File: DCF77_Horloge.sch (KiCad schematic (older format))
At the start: 22 parts, among them J1 USB_B_Micro, J2 Conn_SWD, J3 Conn_Display, J4 Conn_DCF, Q1 AO3401A, U1 MCP73831-2-OT, U2 NCP1117-3.3_SOT223

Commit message: Add pull up for i2c and change layout
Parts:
- added R8, R9: 2K, Resistor_SMD:R_0603_1608Metric_Pad1.05x0.95mm_HandSolder, symbol Device:R
- J1: symbol Connector:USB_B_Micro -> DCF77_Horloge-rescue:USB_B_Micro-Connector
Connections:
- wire segments 54 -> 60
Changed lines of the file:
@@
 	3350 2350 3700 2350
 $Comp
-L Connector:USB_B_Micro J1
+L DCF77_Horloge-rescue:USB_B_Micro-Connector J1
 U 1 1 6115A94F
 P 1050 1900
@@
 	0    1    1    0
 $EndComp
+Text GLabel 8950 1450 2    50   Input ~ 0
+SCL
+Text GLabel 8950 1350 2    50   Input ~ 0
+SDA
+$Comp
+L Device:R R9
+U 1 1 611EA76E
+P 8850 1150
+F 0 "R9" H 8800 1100 50  0000 R CNN
+F 1 "2K" H 8780 1195 50  0000 R CNN
+F 2 "Resistor_SMD:R_0603_1608Metric_Pad1.05x0.95mm_HandSolder" V 8780 1150 50  0001 C CNN
+F 3 "~" H 8850 1150 50  0001 C CNN
+	1    8850 1150
+	-1   0    0    1
+$EndComp
+$Comp
+L Device:R R8
+U 1 1 611EB153
+P 8600 1150
+F 0 "R8" H 8750 1150 50  0000 R CNN
+F 1 "2K" H 8750 1250 50  0000 R CNN
+F 2 "Resistor_SMD:R_0603_1608Metric_Pad1.05x0.95mm_HandSolder" V 8530 1150 50  0001 C CNN
+F 3 "~" H 8600 1150 50  0001 C CNN
+	1    8600 1150
+	-1   0    0    1
+$EndComp
+Wire Wire Line
+	8850 1300 8850 1350
+Wire Wire Line
+	8850 1350 8950 1350
+Wire Wire Line
+	8950 1450 8600 1450
+Wire Wire Line
+	8600 1450 8600 1300
+Wire Wire Line
+	8600 1000 8750 1000
+$Comp
+L power:+3.3V #PWR011
+U 1 1 611EE2A2
+P 8750 1000
+F 0 "#PWR011" H 8750 850 50  0001 C CNN
+F 1 "+3.3V" H 8750 1100 50  0000 L CNN
+F 2 "" H 8750 1000 50  0001 C CNN
+F 3 "" H 8750 1000 50  0001 C CNN
+	1    8750 1000
+	1    0    0    -1
+$EndComp
+Connection ~ 8750 1000
+Wire Wire Line
+	8750 1000 8850 1000
 $EndSCHEMATC

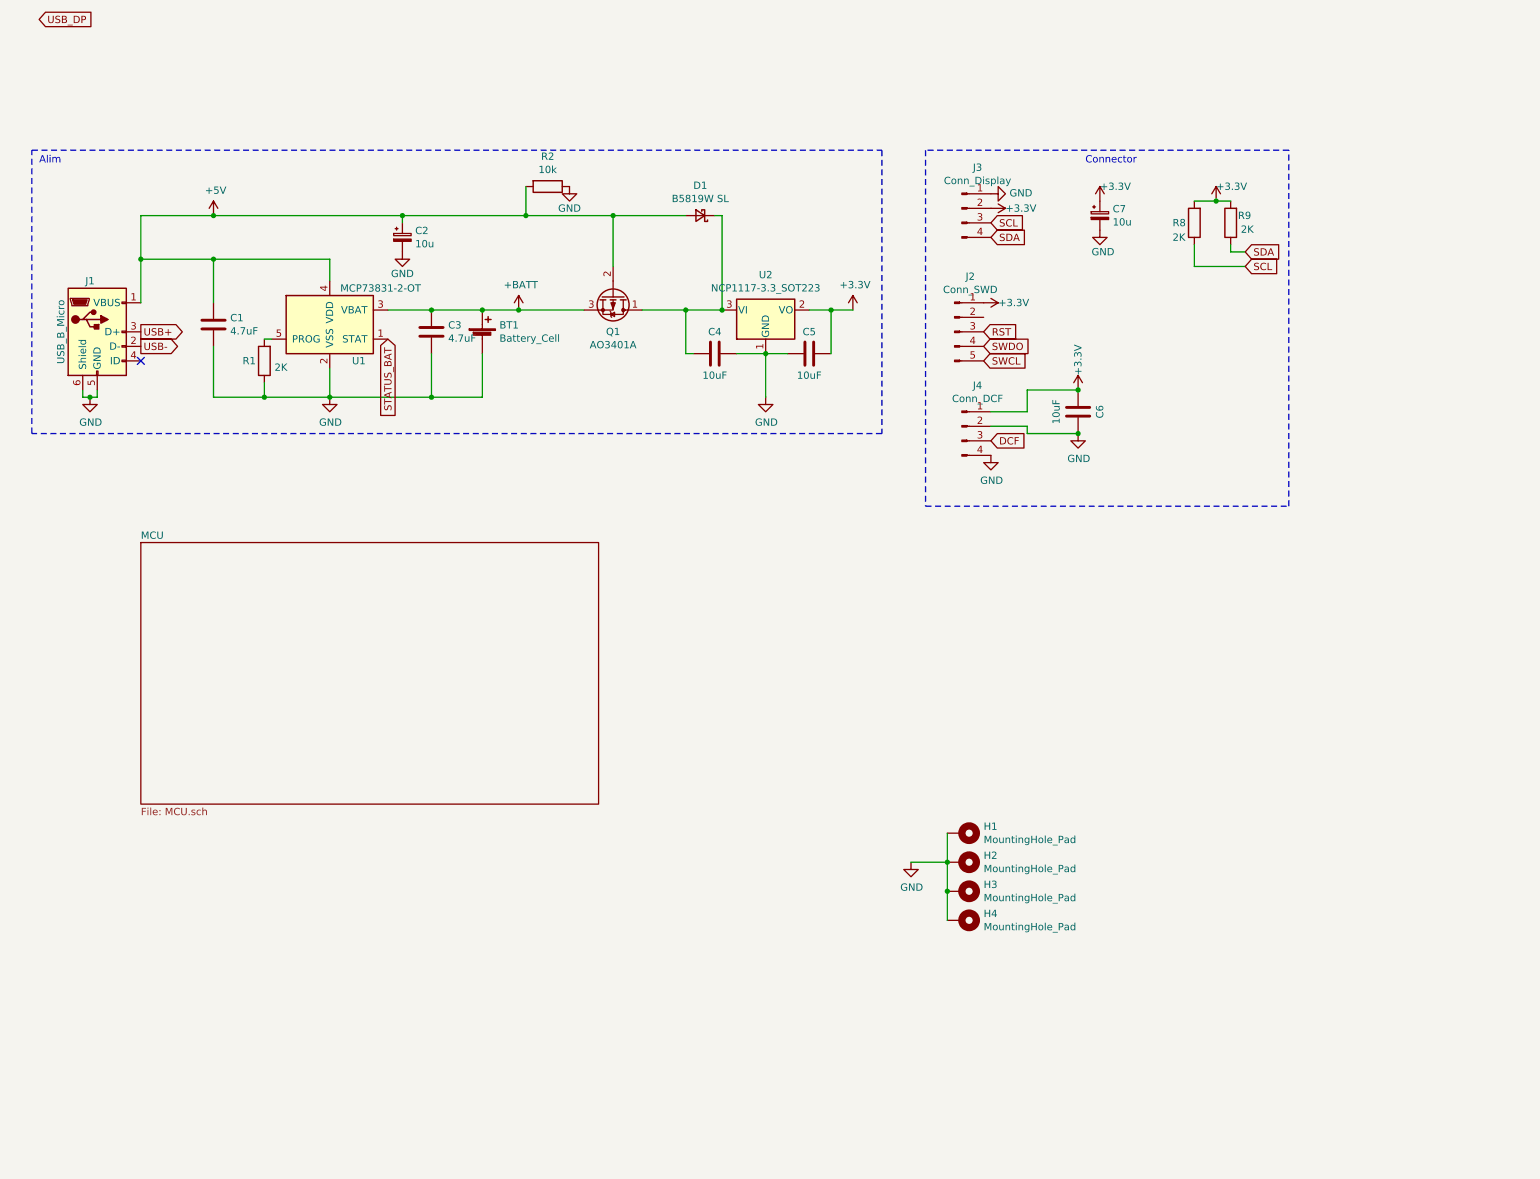
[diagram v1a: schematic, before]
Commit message: change MCU from RP2040 to ESP32-WROOM-32
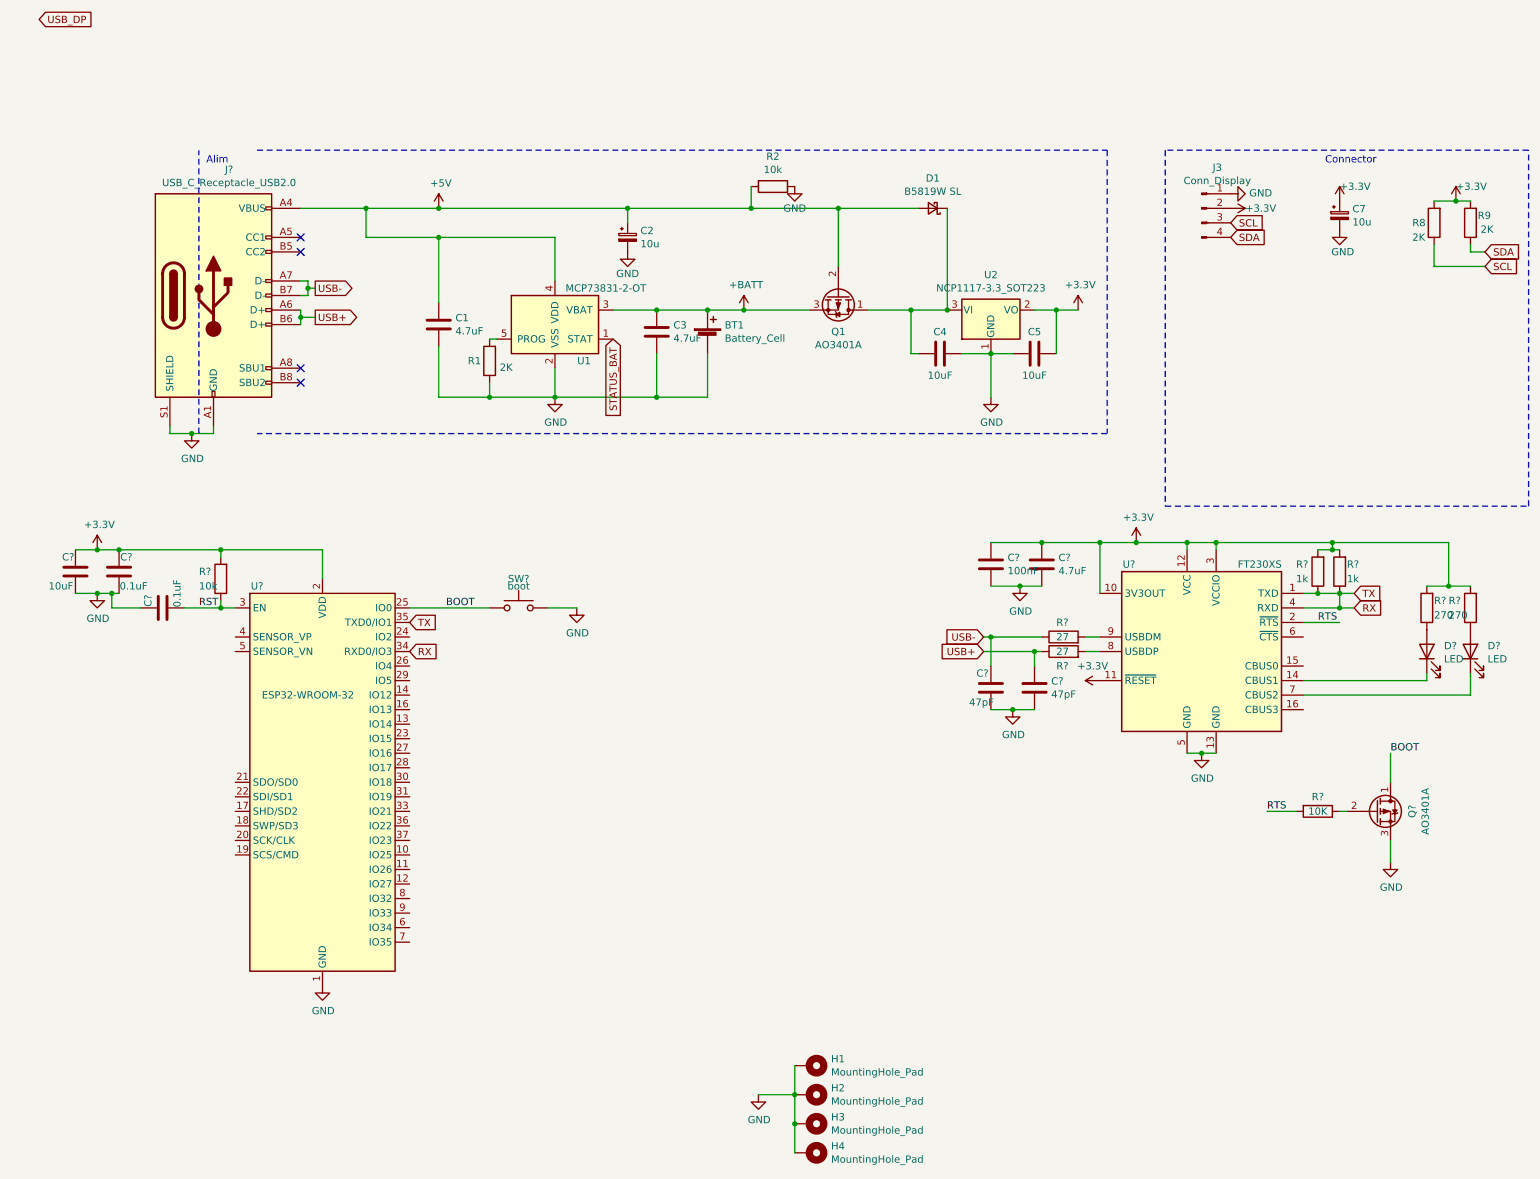
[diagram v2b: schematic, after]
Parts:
- removed C6: 10uF, Capacitor_SMD:C_0603_1608Metric_Pad1.08x0.95mm_HandSolder, symbol Device:C
- removed J1: USB_B_Micro, Connector_USB:USB_Micro-B_Wuerth_629105150521, symbol DCF77_Horloge-rescue:USB_B_Micro-Connector
- removed J2: Conn_SWD, Connector_PinSocket_2.54mm:PinSocket_1x05_P2.54mm_Vertical, symbol Connector:Conn_01x05_Male
- removed J4: Conn_DCF, Connector_PinHeader_2.54mm:PinHeader_1x04_P2.54mm_Vertical, symbol Connector:Conn_01x04_Male
- added C?: 4.7uF, symbol Device:C
- added C?: 100nF, symbol Device:C
- added C? (x2): 47pF, symbol Device:C
- added C?: 10uF, Capacitor_SMD:C_0603_1608Metric_Pad1.08x0.95mm_HandSolder, symbol Device:C
- added C? (x2): 0.1uF, Capacitor_SMD:C_0603_1608Metric_Pad1.08x0.95mm_HandSolder, symbol Device:C
- added D? (x2): LED, symbol Device:LED
- added J?: USB_C_Receptacle_USB2.0, symbol Connector:USB_C_Receptacle_USB2.0
- added Q?: AO3401A, Package_TO_SOT_SMD:SOT-23, symbol Device:Q_PMOS_DGS
- added R? (x2): 1k, Resistor_SMD:R_0603_1608Metric_Pad0.98x0.95mm_HandSolder, symbol Device:R
- added R? (x2): 270, Resistor_SMD:R_0603_1608Metric_Pad0.98x0.95mm_HandSolder, symbol Device:R
- added R? (x2): 27, Resistor_SMD:R_0603_1608Metric_Pad0.98x0.95mm_HandSolder, symbol Device:R
- added R?: 10k, Resistor_SMD:R_0603_1608Metric_Pad0.98x0.95mm_HandSolder, symbol Device:R
- added R?: 10K, symbol Device:R
- added SW?: boot, symbol Switch:SW_Push
- added U?: ESP32-WROOM-32, RF_Module:ESP32-WROOM-32, symbol RF_Module:ESP32-WROOM-32
- added U?: FT230XS, Package_SO:SSOP-16_3.9x4.9mm_P0.635mm, symbol Interface_USB:FT230XS
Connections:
- net +3V3: now also C?.1, C?.1, C?.2, C?.2, R?.2, R?.2, R?.2, R?.2, R?.2, U?.10 (3V3OUT), U?.11 (~RESET), U?.12 (VCC), U?.2 (VDD), U?.3 (VCCIO)
- net +5V: now also J?.A4 (VBUS), J?.A9 (VBUS), J?.B4 (VBUS), J?.B9 (VBUS)
- net GND: now also C?.1, C?.1, C?.2, C?.2, C?.2, C?.2, C?.2, J?.A1 (GND), J?.A12 (GND), J?.B1 (GND), J?.B12 (GND), J?.S1 (SHIELD), Q?.3 (S), SW?.2, U?.1 (GND), U?.13 (GND), U?.15 (GND), U?.38 (GND), U?.39 (GND), U?.5 (GND)
- net RST: now also C?.1, R?.1, U?.3 (EN)
- net USB+: now also C?.1, J?.A6 (D+), J?.B6 (D+), R?.1
- net USB-: now also C?.1, J?.A7 (D-), J?.B7 (D-), R?.1
- new net: D?.1 (K), U?.14 (CBUS1)
- new net: D?.1 (K), U?.7 (CBUS2)
- new net: R?.2, U?.8 (USBDP)
- new net: R?.2, U?.9 (USBDM)
- new net: D?.2 (A), R?.1 (x2)
- new net: Q?.2 (G), R?.1
- new net BOOT: Q?.1 (D), SW?.1, U?.25 (IO0)
- new net RTS: R?.2, U?.2 (~RTS)
- new net RX: R?.1, R?.1, U?.1 (TXD), U?.34 (RXD0/IO3), U?.35 (TXD0/IO1), U?.4 (RXD)
- no-connect marks 1 -> 4
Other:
- moved on the sheet: BT1, C1, C2, C3, C4, C5, C7, D1, H1, H2, H3, H4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

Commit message: mod with esp 32
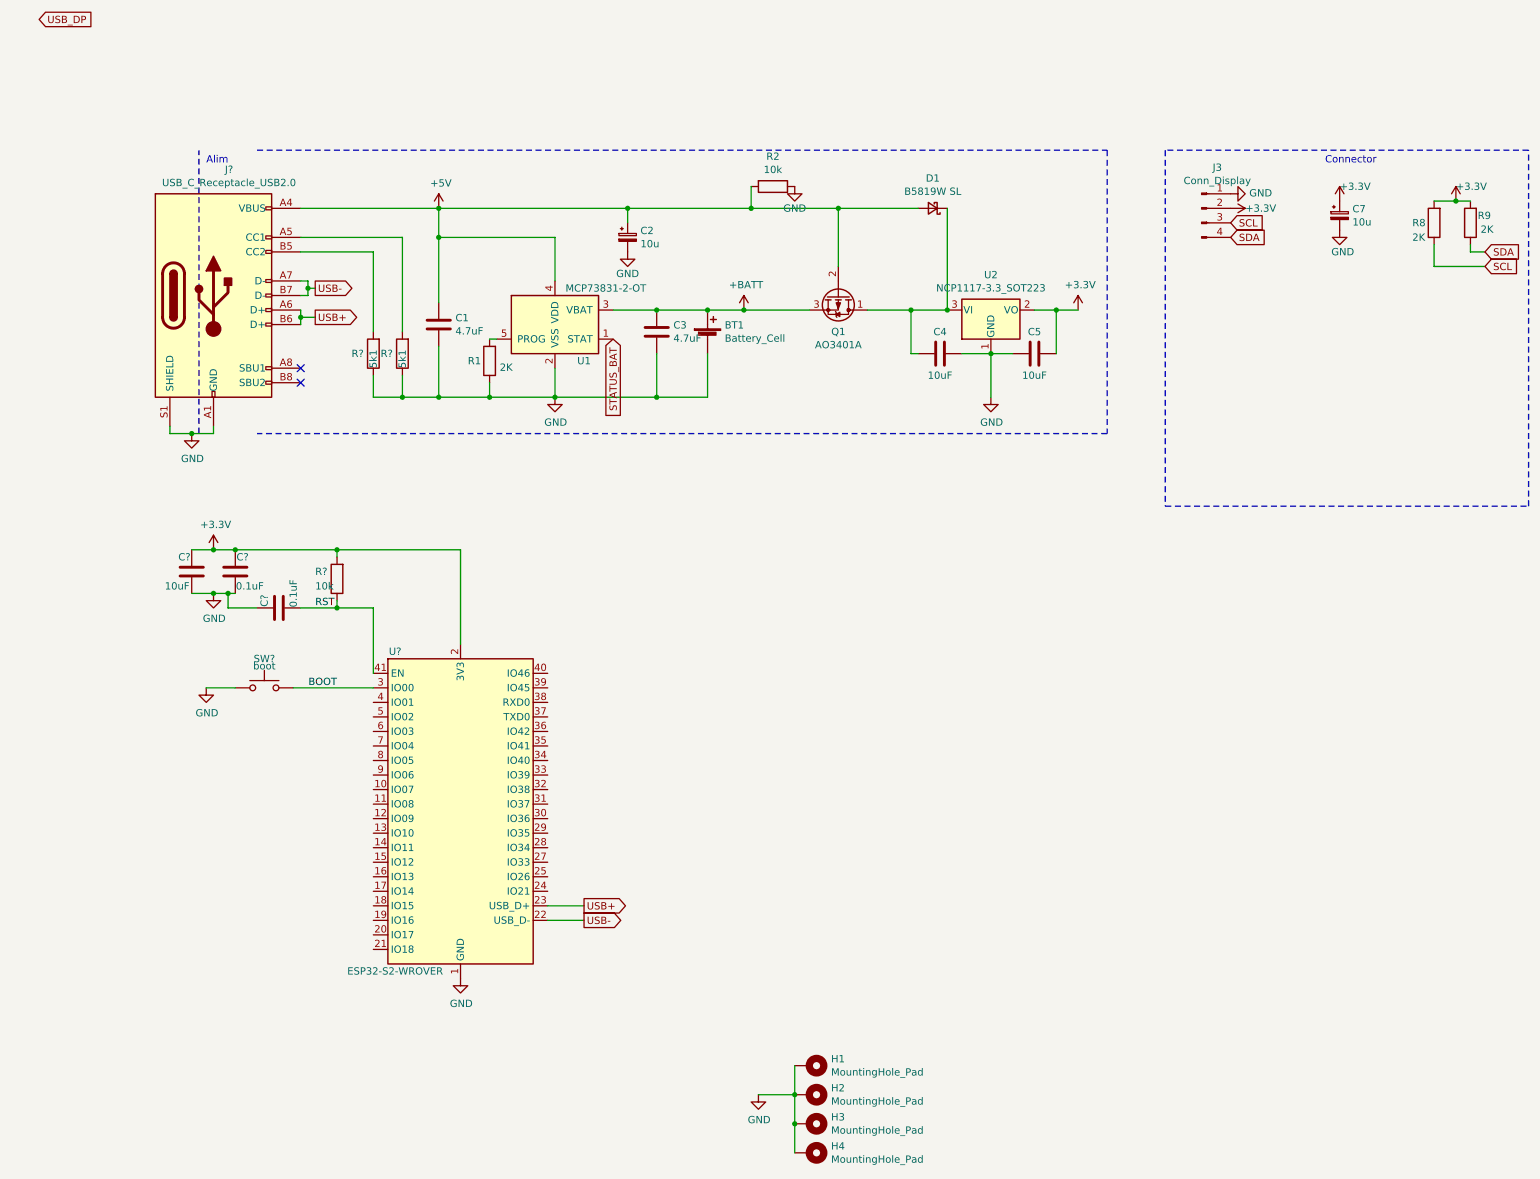
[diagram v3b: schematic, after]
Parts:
- removed C?: 4.7uF, symbol Device:C
- removed C?: 100nF, symbol Device:C
- removed C? (x2): 47pF, symbol Device:C
- removed D? (x2): LED, symbol Device:LED
- removed Q?: AO3401A, Package_TO_SOT_SMD:SOT-23, symbol Device:Q_PMOS_DGS
- removed R? (x2): 1k, Resistor_SMD:R_0603_1608Metric_Pad0.98x0.95mm_HandSolder, symbol Device:R
- removed R? (x2): 270, Resistor_SMD:R_0603_1608Metric_Pad0.98x0.95mm_HandSolder, symbol Device:R
- removed R? (x2): 27, Resistor_SMD:R_0603_1608Metric_Pad0.98x0.95mm_HandSolder, symbol Device:R
- removed R?: 10K, symbol Device:R
- removed U?: ESP32-WROOM-32, RF_Module:ESP32-WROOM-32, symbol RF_Module:ESP32-WROOM-32
- removed U?: FT230XS, Package_SO:SSOP-16_3.9x4.9mm_P0.635mm, symbol Interface_USB:FT230XS
- added R? (x2): 5k1, Resistor_SMD:R_0603_1608Metric_Pad0.98x0.95mm_HandSolder, symbol Device:R
- added U?: ESP32-S2-WROVER, RF_Module:ESP32-S2-WROVER, symbol RF_Module:ESP32-S2-WROVER
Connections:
- net +3V3: now also U?.2 (3V3)
- net BOOT: now also SW?.2, U?.3 (IO00); no longer SW?.1
- net GND: now also SW?.1, R?.1, R?.1, U?.1 (GND), U?.26 (GND), U?.42 (GND), U?.43 (GND); no longer SW?.2
- net RST: now also U?.41 (EN)
- net USB+: now also U?.23 (USB_D+)
- net USB-: now also U?.22 (USB_D-)
- net at J?.A5 (CC1): now also R?.2
- net at J?.B5 (CC2): now also R?.2
- no-connect marks 4 -> 2
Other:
- moved on the sheet: C?, R?, SW?
